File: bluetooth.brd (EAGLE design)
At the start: 28.3 x 23.1 mm, 28 parts, among them U1 NRF8001, X1 16MHz, X2 32.768kHz

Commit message: fix readme
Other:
- board text added: "Attribution-ShareAlike 3.0"
- board text added: "Creative Commons"
- board text added: "Unported License"
- board text added: "www.nabiltewolde.com"
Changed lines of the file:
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@@
 <layer number="24" name="bOrigins" color="15" fill="1" visible="yes" active="yes"/>
 <layer number="25" name="tNames" color="7" fill="1" visible="yes" active="yes"/>
-<layer number="26" name="bNames" color="7" fill="1" visible="no" active="yes"/>
+<layer number="26" name="bNames" color="7" fill="1" visible="yes" active="yes"/>
 <layer number="27" name="tValues" color="7" fill="1" visible="no" active="yes"/>
 <layer number="28" name="bValues" color="7" fill="1" visible="no" active="yes"/>
@@
 <text x="23.9952125" y="6.200003125" size="1.016" layer="26" rot="MR0">GND</text>
 <text x="20.7999875" y="2.1692" size="1.016" layer="26" rot="MR180">3.3V</text>
+<text x="26.5176" y="8.2296" size="1.27" layer="26" rot="MR0">Creative Commons</text>
+<text x="26.5176" y="11.5824" size="1.27" layer="26" rot="MR0">Attribution-ShareAlike 3.0</text>
+<text x="26.5176" y="10.0584" size="1.27" layer="26" rot="MR0">Unported License</text>
+<text x="16.9164" y="0.3048" size="1.016" layer="26" rot="MR0">www.nabiltewolde.com</text>
 </plain>
 <attributes>

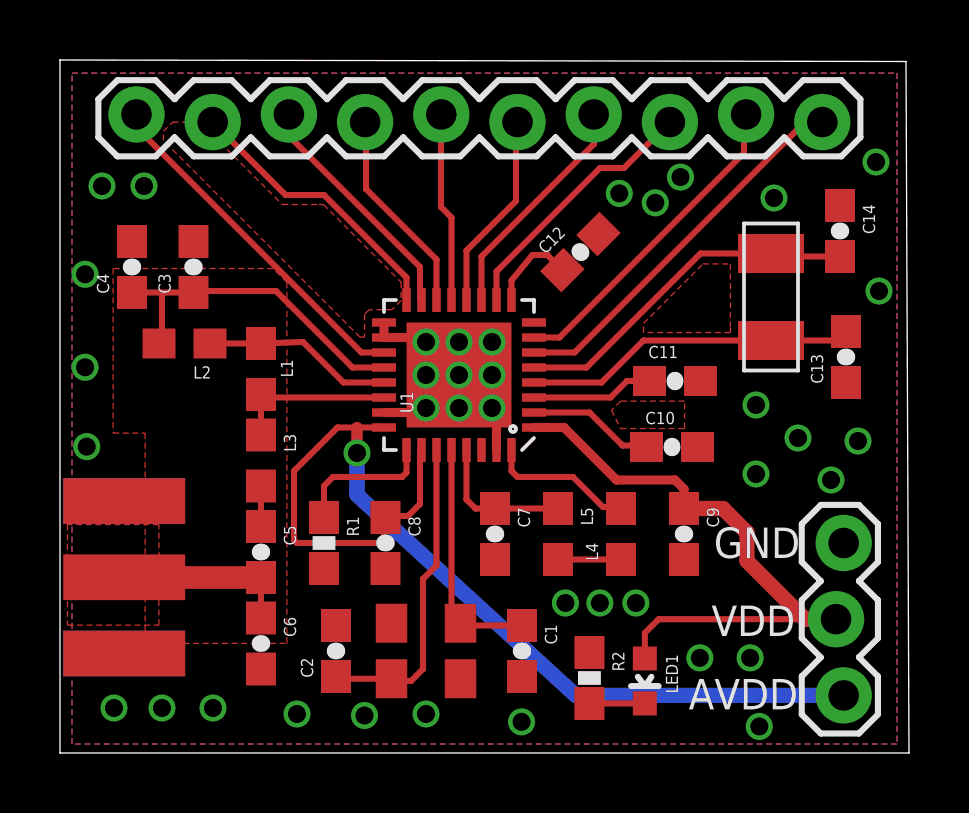
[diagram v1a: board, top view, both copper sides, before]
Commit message: updated BOM, fixed 32kHz crystal footprint and added datasheet
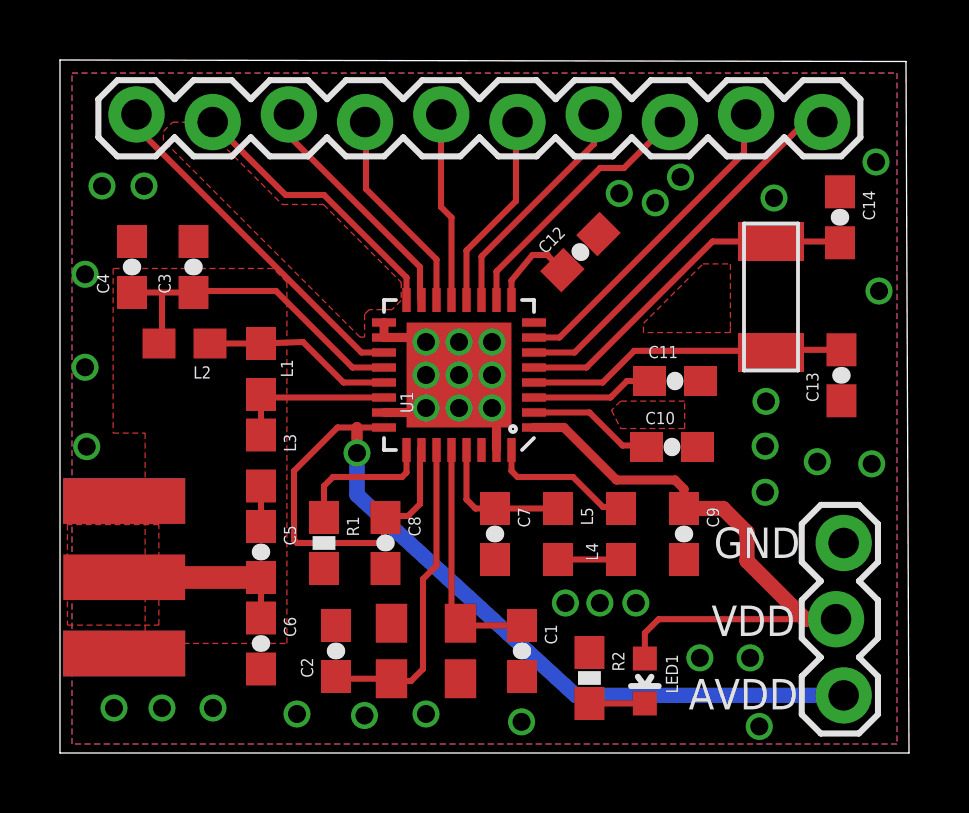
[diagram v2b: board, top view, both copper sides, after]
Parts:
- moved C13 0.63 mm to (25.6, 12.3)
- moved C14 0.46 mm to (25.6, 17.6)
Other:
- board text added: "CC-BY-SA"
- board text removed: "Attribution-ShareAlike 3.0"
- board text removed: "Creative Commons"
- board text removed: "Unported License"
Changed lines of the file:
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@@
 <setting verticaltext="up"/>
 </settings>
-<grid distance="6" unitdist="mil" unit="mm" style="lines" multiple="1" display="yes" altdistance="0.05" altunitdist="mm" altunit="mm"/>
+<grid distance="6" unitdist="mil" unit="mil" style="lines" multiple="1" display="yes" altdistance="0.05" altunitdist="mm" altunit="mm"/>
 <layers>
-<layer number="1" name="Top" color="4" fill="1" visible="yes" active="yes"/>
+<layer number="1" name="Top" color="4" fill="1" visible="no" active="yes"/>
 <layer number="16" name="Bottom" color="1" fill="1" visible="yes" active="yes"/>
 <layer number="17" name="Pads" color="2" fill="1" visible="yes" active="yes"/>
@@
 <layer number="106" name="bPlate" color="7" fill="1" visible="no" active="yes"/>
 <layer number="107" name="Crop" color="7" fill="1" visible="no" active="yes"/>
+<layer number="116" name="Patch_BOT" color="9" fill="4" visible="no" active="yes"/>
 <layer number="121" name="_tsilk" color="7" fill="1" visible="no" active="yes"/>
 <layer number="122" name="_bsilk" color="7" fill="1" visible="no" active="yes"/>
@@
 <layer number="220" name="220bmp" color="21" fill="1" visible="no" active="no"/>
 <layer number="221" name="221bmp" color="22" fill="1" visible="no" active="no"/>
+<layer number="222" name="222bmp" color="23" fill="1" visible="no" active="no"/>
 <layer number="223" name="223bmp" color="24" fill="1" visible="no" active="no"/>
 <layer number="224" name="224bmp" color="25" fill="1" visible="no" active="no"/>
@@
 <text x="23.9952125" y="6.200003125" size="1.016" layer="26" rot="MR0">GND</text>
 <text x="20.7999875" y="2.1692" size="1.016" layer="26" rot="MR180">3.3V</text>
-<text x="26.5176" y="8.2296" size="1.27" layer="26" rot="MR0">Creative Commons</text>
-<text x="26.5176" y="11.5824" size="1.27" layer="26" rot="MR0">Attribution-ShareAlike 3.0</text>
-<text x="26.5176" y="10.0584" size="1.27" layer="26" rot="MR0">Unported License</text>
-<text x="16.9164" y="0.3048" size="1.016" layer="26" rot="MR0">www.nabiltewolde.com</text>
+<text x="20.574" y="7.7724" size="1.016" layer="26" rot="MR0">www.nabiltewolde.com</text>
+<text x="16.1544" y="5.7912" size="1.016" layer="26" rot="MR0">CC-BY-SA</text>
 </plain>
 <attributes>
@@
 <element name="C10" library="SparkFun" package="0603-CAP" value="100nF" x="20.000009375" y="9.90000625"/>
 <element name="C11" library="SparkFun" package="0603-CAP" value="33nF" x="20.100009375" y="12.10000625"/>
-<element name="C13" library="SparkFun" package="0603-CAP" value="12.5pF" x="25.8000125" y="12.90000625" rot="R90"/>
-<element name="C14" library="SparkFun" package="0603-CAP" value="12.5pF" x="25.6000125" y="17.100009375" rot="R270"/>
+<element name="C13" library="SparkFun" package="0603-CAP" value="12.5pF" x="25.6476125" y="12.29040625" rot="R90"/>
+<element name="C14" library="SparkFun" package="0603-CAP" value="12.5pF" x="25.6000125" y="17.557209375" rot="R270"/>
 <element name="C12" library="SparkFun" package="0603-CAP" value="100nF" x="16.9476" y="16.3976" rot="R45"/>
 <element name="C3" library="SparkFun" package="0603-CAP" value="2.2nF" x="4.05" y="15.9" rot="R90"/>
@@
 <via x="18.242809375" y="18.352409375" extent="1-16" drill="0.6"/>
 <via x="19.442809375" y="18.038009375" extent="1-16" drill="0.6"/>
-<via x="24.200015625" y="10.20000625" extent="1-16" drill="0.6"/>
-<via x="26.200015625" y="10.10000625" extent="1-16" drill="0.6"/>
-<via x="22.8000125" y="11.30000625" extent="1-16" drill="0.6"/>
-<via x="22.8000125" y="9.00000625" extent="1-16" drill="0.6"/>
+<via x="23.133215625" y="11.41920625" extent="1-16" drill="0.6"/>
+<via x="26.657215625" y="9.33800625" extent="1-16" drill="0.6"/>
+<via x="23.1048125" y="9.92840625" extent="1-16" drill="0.6"/>
+<via x="23.1048125" y="8.39040625" extent="1-16" drill="0.6"/>
 <via x="1" y="18.600009375" extent="1-16" drill="0.6"/>
 <via x="23.4000125" y="18.200009375" extent="1-16" drill="0.6"/>
@@
 <wire x1="10.40000625" y1="14.05000625" x2="10.40000625" y2="13.55000625" width="0.3048" layer="1"/>
 <via x="2.4" y="18.600009375" extent="1-16" drill="0.6"/>
-<via x="25.3000125" y="8.800003125" extent="1-16" drill="0.6"/>
+<via x="24.8428125" y="9.409603125" extent="1-16" drill="0.6"/>
 <via x="11.80000625" y="1" extent="1-16" drill="0.6"/>
 <via x="26.800015625" y="19.400009375" extent="1-16" drill="0.6"/>
@@
 <contactref element="U1" pad="4"/>
 <contactref element="X2" pad="P$2"/>
-<wire x1="15.40000625" y1="12.05000625" x2="17.65000625" y2="12.05000625" width="0.2032" layer="1"/>
-<wire x1="17.65000625" y1="12.05000625" x2="19.05" y2="13.45" width="0.2032" layer="1"/>
-<wire x1="19.05" y1="13.45" x2="23.300003125" y2="13.45" width="0.2032" layer="1"/>
-<wire x1="23.300003125" y1="13.45" x2="23.3000125" y2="13.450009375" width="0.2032" layer="1"/>
-<wire x1="23.3000125" y1="13.450009375" x2="25.500015625" y2="13.450009375" width="0.2032" layer="1"/>
-<wire x1="25.500015625" y1="13.450009375" x2="25.8000125" y2="13.75000625" width="0.2032" layer="1"/>
+<wire x1="15.40000625" y1="12.05000625" x2="17.68880625" y2="12.05000625" width="0.2032" layer="1"/>
+<wire x1="23.300003125" y1="13.45" x2="23.3000125" y2="13.050009375" width="0.2032" layer="1"/>
+<wire x1="17.68880625" y1="12.05000625" x2="18.7452" y2="13.1064" width="0.2032" layer="1"/>
+<wire x1="18.7452" y1="13.1064" x2="23.243621875" y2="13.1064" width="0.2032" layer="1"/>
+<wire x1="23.243621875" y1="13.1064" x2="23.3000125" y2="13.050009375" width="0.2032" layer="1"/>
+<wire x1="25.6476125" y1="13.14040625" x2="23.390409375" y2="13.14040625" width="0.2032" layer="1"/>
+<wire x1="23.390409375" y1="13.14040625" x2="23.3000125" y2="13.050009375" width="0.2032" layer="1"/>
 </signal>
 <signal name="N$18">
@@
 <contactref element="X2" pad="P$1"/>
 <wire x1="15.40000625" y1="12.55000625" x2="17.15000625" y2="12.55000625" width="0.2032" layer="1"/>
-<wire x1="23.3000125" y1="16.350009375" x2="20.950009375" y2="16.350009375" width="0.2032" layer="1"/>
-<wire x1="25.6000125" y1="16.250009375" x2="23.4000125" y2="16.250009375" width="0.2032" layer="1"/>
-<wire x1="23.4000125" y1="16.250009375" x2="23.3000125" y2="16.350009375" width="0.2032" layer="1"/>
-<wire x1="20.950009375" y1="16.350009375" x2="17.15000625" y2="12.55000625" width="0.2032" layer="1"/>
+<wire x1="21.35" y1="16.75" x2="17.15000625" y2="12.55000625" width="0.2032" layer="1"/>
+<wire x1="21.35" y1="16.75" x2="23.300003125" y2="16.75" width="0.2032" layer="1"/>
+<wire x1="23.300003125" y1="16.75" x2="23.3000125" y2="16.750009375" width="0.2032" layer="1"/>
+<wire x1="23.3000125" y1="16.750009375" x2="25.5572125" y2="16.750009375" width="0.2032" layer="1"/>
+<wire x1="25.5572125" y1="16.750009375" x2="25.6000125" y2="16.707209375" width="0.2032" layer="1"/>
 </signal>
 <signal name="N$19">

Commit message: small DRC fix, added gerber files
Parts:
- moved J$1 0.15 mm to (1.89, 8.10)
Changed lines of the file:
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@@
 <setting verticaltext="up"/>
 </settings>
-<grid distance="6" unitdist="mil" unit="mil" style="lines" multiple="1" display="yes" altdistance="0.05" altunitdist="mm" altunit="mm"/>
+<grid distance="6" unitdist="mil" unit="inch" style="lines" multiple="1" display="yes" altdistance="0.05" altunitdist="mm" altunit="mm"/>
 <layers>
-<layer number="1" name="Top" color="4" fill="1" visible="no" active="yes"/>
+<layer number="1" name="Top" color="4" fill="1" visible="yes" active="yes"/>
 <layer number="16" name="Bottom" color="1" fill="1" visible="yes" active="yes"/>
 <layer number="17" name="Pads" color="2" fill="1" visible="yes" active="yes"/>
@@
 <element name="LED1" library="SparkFun" package="LED-0603" value="" x="19.095209375" y="2.1" rot="R180"/>
 <element name="R2" library="SparkFun" package="0603-RES" value="" x="17.247609375" y="2.2" rot="R270"/>
-<element name="J$1" library="SparkFun" package="SMA-EDGE" value="SMA_EDGE" x="1.7404" y="8.0976" rot="R270"/>
+<element name="J$1" library="SparkFun" package="SMA-EDGE" value="SMA_EDGE" x="1.8928" y="8.0976" rot="R270"/>
 <element name="JP3" library="SparkFun" package="1X10_LOCK" value="M10LOCK" x="2.149996875" y="20.857959375" smashed="yes"/>
 </elements>
@@
 <wire x1="6.3" y1="5.55" x2="6.3" y2="4.2" width="0.2032" layer="1"/>
 <wire x1="6.3" y1="5.55" x2="2.06" y2="5.55" width="0.762" layer="1"/>
-<wire x1="2.06" y1="5.55" x2="1.7404" y2="5.5576" width="0.762" layer="1"/>
+<wire x1="2.06" y1="5.55" x2="1.8928" y2="5.5576" width="0.762" layer="1"/>
 </signal>
 <signal name="N$12">
@@
 <vertex x="21.0312" y="16.002"/>
 </polygon>
+<polygon width="0.2032" layer="1">
+<vertex x="7.4676" y="11.1252"/>
+<vertex x="7.4676" y="9.906"/>
+<vertex x="7.7724" y="9.906"/>
+<vertex x="8.6868" y="10.8204"/>
+<vertex x="10.0584" y="10.8204"/>
+<vertex x="10.2108" y="10.8204"/>
+<vertex x="10.2108" y="11.1252"/>
+</polygon>
+<polygon width="0.2032" layer="1">
+<vertex x="10.9728" y="12.8016"/>
+<vertex x="10.9728" y="11.5824"/>
+<vertex x="11.0324" y="11.5824"/>
+<vertex x="11.05" y="11.6"/>
+<vertex x="11.05" y="12.8"/>
+</polygon>
+<polygon width="0.2032" layer="1">
+<vertex x="12.15" y="14.15"/>
+<vertex x="13.55" y="14.15"/>
+<vertex x="13.55" y="14.2"/>
+<vertex x="12.15" y="14.2"/>
+</polygon>
+<polygon width="0.2032" layer="1">
+<vertex x="14.7" y="11.45"/>
+<vertex x="14.7" y="13.35"/>
+<vertex x="14.8" y="13.35"/>
+<vertex x="14.8" y="11.45"/>
+</polygon>
+<polygon width="0.2032" layer="1">
+<vertex x="12.15" y="10.5"/>
+<vertex x="13.65" y="10.5"/>
+<vertex x="13.65" y="10.45"/>
+<vertex x="12.15" y="10.45"/>
+</polygon>
 </signal>
 <signal name="AVDD">
@@
 <contactref element="C8" pad="1"/>
 <contactref element="U1" pad="24"/>
-<wire x1="11.60000625" y1="9.85000625" x2="11.65000625" y2="9.80000625" width="0.2032" layer="1"/>
-<wire x1="11.60000625" y1="9.85000625" x2="11.60000625" y2="8.00000625" width="0.2032" layer="1"/>
-<wire x1="11.60000625" y1="8.00000625" x2="11.2" y2="7.6" width="0.2032" layer="1"/>
-<wire x1="11.2" y1="7.6" x2="10.45" y2="7.6" width="0.2032" layer="1"/>
 <wire x1="10.45" y1="7.6" x2="10.45" y2="7.55" width="0.2032" layer="1"/>
-<wire x1="10.40000625" y1="10.55000625" x2="9.50000625" y2="10.55000625" width="0.2032" layer="1"/>
-<wire x1="9.50000625" y1="10.55000625" x2="8.850003125" y2="10.55000625" width="0.2032" layer="1"/>
-<wire x1="8.850003125" y1="10.55000625" x2="7.400003125" y2="9.10000625" width="0.2032" layer="1"/>
-<wire x1="7.400003125" y1="9.10000625" x2="7.400003125" y2="6.800003125" width="0.2032" layer="1"/>
-<wire x1="7.400003125" y1="6.800003125" x2="7.500003125" y2="6.700003125" width="0.2032" layer="1"/>
-<wire x1="7.500003125" y1="6.700003125" x2="10.20000625" y2="6.700003125" width="0.2032" layer="1"/>
-<wire x1="10.20000625" y1="6.700003125" x2="10.40000625" y2="6.900003125" width="0.2032" layer="1"/>
-<wire x1="10.40000625" y1="6.900003125" x2="10.40000625" y2="7.54999375" width="0.2032" layer="1"/>
+<wire x1="10.40000625" y1="10.55000625" x2="9.7536" y2="10.55000625" width="0.2032" layer="1"/>
 <wire x1="10.40000625" y1="7.54999375" x2="10.45" y2="7.55" width="0.2032" layer="1"/>
 <wire x1="25.722209375" y1="1.62000625" x2="16.789603125" y2="1.62000625" width="0.508" layer="16"/>
@@
 <wire x1="9.50000625" y1="8.300003125" x2="9.50000625" y2="9.70000625" width="0.508" layer="16"/>
 <via x="9.50000625" y="9.70000625" extent="1-16" drill="0.6"/>
-<wire x1="9.50000625" y1="9.70000625" x2="9.50000625" y2="10.55000625" width="0.381" layer="1"/>
+<wire x1="9.50000625" y1="9.70000625" x2="9.50000625" y2="10.2964125" width="0.254" layer="1"/>
+<wire x1="9.50000625" y1="10.2964125" x2="9.7536" y2="10.55000625" width="0.254" layer="1"/>
+<wire x1="9.7536" y1="10.55000625" x2="8.87360625" y2="10.55000625" width="0.254" layer="1"/>
+<wire x1="8.87360625" y1="10.55000625" x2="7.4676" y2="9.144" width="0.254" layer="1"/>
+<wire x1="7.4676" y1="9.144" x2="7.4676" y2="6.858" width="0.254" layer="1"/>
+<wire x1="7.4676" y1="6.858" x2="7.62" y2="6.7056" width="0.254" layer="1"/>
+<wire x1="7.62" y1="6.7056" x2="10.2556" y2="6.7056" width="0.254" layer="1"/>
+<wire x1="10.2556" y1="6.7056" x2="10.45" y2="6.9" width="0.254" layer="1"/>
+<wire x1="10.45" y1="6.9" x2="10.45" y2="7.55" width="0.254" layer="1"/>
+<wire x1="11.65000625" y1="9.80000625" x2="11.65000625" y2="7.84000625" width="0.254" layer="1"/>
+<wire x1="11.65000625" y1="7.84000625" x2="11.2776" y2="7.4676" width="0.254" layer="1"/>
+<wire x1="11.2776" y1="7.4676" x2="10.5324" y2="7.4676" width="0.254" layer="1"/>
+<wire x1="10.5324" y1="7.4676" x2="10.45" y2="7.55" width="0.254" layer="1"/>
 </signal>
 <signal name="N$5">
